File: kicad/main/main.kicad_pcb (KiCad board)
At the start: 2 copper layers, 20 parts, among them U1 DS1813-5+, U2 L7805, U3 Z80CPU, U4 74HC00, U5 AS6C4008-55PCN, U6 74HC273, U7 27C512, X1 4 MHz

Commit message: Smaller KiCad symbols, reset button
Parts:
- added SW1: Reset, Button_Switch_THT:SW_PUSH_6mm, F.Cu at (37.4, 99.3)
- added U5: 74HC00, Package_DIP:DIP-14_W7.62mm_Socket, F.Cu at (76.2, 114.3)
- moved C1 18.9 mm to (40.1, 45.7), turned to 180 degrees
- moved C4 12.8 mm to (119.4, 111.7)
- moved U4 12.8 mm to (99.1, 114.3)
- moved C2 2.58 mm to (30.5, 45.7)
- renumbered U5 to U6, U6 to U7, U7 to U8
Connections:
- U3 pad 27: unconnected-(U3-~{M1}-Pad27) -> ~{M1}
- U7 pad 11: ~{IORQ} -> IO~{EN}

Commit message: Basic PCB
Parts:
- added J1: Barrel_Jack_MountingPin, Connector_BarrelJack:BarrelJack_GCT_DCJ200-10-A_Horizontal, F.Cu at (157.2, 39.7)
- added RN3: 5K, Resistor_THT:R_Array_SIP9, F.Cu at (134.6, 106.7)
- added SW2: SW_DIP_x08, Button_Switch_THT:SW_DIP_SPSTx08_Slide_9.78x22.5mm_W7.62mm_P2.54mm, F.Cu at (137.2, 119.3)
- added U1: 74HC00, Package_DIP:DIP-14_W7.62mm_Socket, F.Cu at (86.4, 104.1)
- added U10: 74HC244, Package_DIP:DIP-20_W7.62mm_Socket, F.Cu at (134.5, 101.5)
- U9: renamed from U8; footprint Package_DIP:DIP-28_W15.24mm -> my:ZIF28
- moved C1 117.0 mm to (147.3, 38.1), turned to 180 degrees
- moved U7 107.0 mm to (139.7, 30.5)
- moved C9 97.4 mm to (137.2, 38.1), turned to 0 degrees
- moved X1 87.6 mm to (111.8, 90.2)
- moved C7 65.2 mm to (76.2, 91.4), turned to 180 degrees
- moved RN1 58.9 mm to (104.1, 88.9), turned to 180 degrees
- moved C8 48.4 mm to (73.7, 109.2)
- moved U5 48.4 mm to (73.7, 101.6)
- moved U4 45.4 mm to (94.0, 27.9)
- moved C2 45.4 mm to (99.1, 81.3)
- moved C4 43.1 mm to (121.9, 71.1), turned to 180 degrees
- moved U6 41.0 mm to (114.3, 27.9)
- moved BAR1 40.2 mm to (134.6, 86.4), turned to 90 degrees
- moved SW1 38.2 mm to (72.2, 114.9)
- moved RN2 37.8 mm to (134.6, 73.7), turned to 0 degrees
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- renumbered C2 to C1, C3 to C2, C4 to C3, C5 to C4, C6 to C5, C7 to C6, C8 to C7, C9 to C8, C1 to C9, U5 to U2, U4 to U3, U3 to U4, U1 to U5, U2 to U7, U7 to U8
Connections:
- net +9V renamed Net-(U7-IN)
- SW1 pad 1: unconnected-(SW1-Pad1) -> ~{RES}
- SW1 pad 2: ~{RES} -> GND
- U8 pad 11: IO~{EN} -> OUT~{EN}
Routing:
- net +5V: track 0.00 -> 159.2 mm
- net GND: track 0.00 -> 156.1 mm
- net Net-(U7-IN): track 0.00 -> 8.67 mm
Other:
- board outline added: 99.1 x 99.1 mm

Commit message: First PCB
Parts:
- removed U10: 74HC244, Package_DIP:DIP-20_W7.62mm_Socket
- removed U9: 27C512, my:ZIF28
- C1, C3, C4, C6, C7, C8: footprint Capacitor_THT:C_Disc_D3.0mm_W1.6mm_P2.50mm -> my:C_Disc_Long
- C2: footprint Capacitor_THT:C_Disc_D3.0mm_W1.6mm_P2.50mm -> my:C_Disc_Medium
- U1: value 74HC00 -> GAL16V8; footprint Package_DIP:DIP-14_W7.62mm_Socket -> Package_DIP:DIP-20_W7.62mm_Socket
- U2: value 74HC00 -> Z80CPU; footprint Package_DIP:DIP-14_W7.62mm_Socket -> Package_DIP:DIP-40_W15.24mm_Socket
- U3: value 74HC00 -> DS1813-5+; footprint Package_DIP:DIP-14_W7.62mm_Socket -> Package_TO_SOT_THT:TO-92
- U4: value Z80CPU -> AS6C4008-55PCN; footprint Package_DIP:DIP-40_W15.24mm_Socket -> Package_DIP:DIP-32_W15.24mm
- U5: value DS1813-5+ -> L7805; footprint Package_TO_SOT_THT:TO-92 -> Package_TO_SOT_THT:TO-220-3_Vertical
- U6: value AS6C4008-55PCN -> 74HC273; footprint Package_DIP:DIP-32_W15.24mm -> Package_DIP:DIP-20_W7.62mm_Socket
- U7: value L7805 -> 27C512; footprint Package_TO_SOT_THT:TO-220-3_Vertical -> my:ZIF28
- U8: value 74HC273 -> 74HC244
- moved U5 98.1 mm to (142.2, 31.4)
- moved U2 92.3 mm to (96.5, 27.9), turned to 0 degrees
- moved U6 76.2 mm to (100.3, 102.9), turned to 90 degrees
- moved U7 70.3 mm to (69.8, 38.1)
- moved C8 63.0 mm to (135.9, 99.1)
- moved U1 50.7 mm to (133.3, 85.1), turned to 90 degrees
- moved BAR1 48.5 mm to (100.3, 120.7)
- moved RN2 48.5 mm to (100.3, 108.0)
- moved C3 46.9 mm to (74.9, 99.1), turned to 0 degrees
- moved C1 44.7 mm to (135.9, 81.3), turned to 0 degrees
- moved U3 43.8 mm to (74.9, 116.8)
- moved X1 40.2 mm to (73.7, 102.9)
- moved U8 36.9 mm to (133.3, 102.9)
- moved C4 30.9 mm to (127.0, 40.6), turned to -90 degrees
- moved C2 27.9 mm to (99.1, 53.3)
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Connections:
- BAR1 pad 1: Net-(U8-Q0) -> Net-(U6-Q0)
- BAR1 pad 2: Net-(U8-Q1) -> Net-(U6-Q1)
- BAR1 pad 3: Net-(U8-Q2) -> Net-(U6-Q2)
- BAR1 pad 4: Net-(U8-Q3) -> Net-(U6-Q3)
- BAR1 pad 5: Net-(U8-Q4) -> Net-(U6-Q4)
- BAR1 pad 6: Net-(U8-Q5) -> Net-(U6-Q5)
- BAR1 pad 7: Net-(U8-Q6) -> Net-(U6-Q6)
- BAR1 pad 8: Net-(U8-Q7) -> Net-(U6-Q7)
- C9 pad 1: Net-(U7-IN) -> Net-(U5-IN)
- J1 pad 1: Net-(U7-IN) -> Net-(U5-IN)
- U1 pad 1: IO~{EN} -> unconnected-(U1-I1/CLK-Pad1)
- U1 pad 10: A_{0} -> GND
- U1 pad 11: OUT~{EN} -> GND
- U1 pad 12: A_{0} -> ROM~{EN}
- U1 pad 13: Net-(U1-Pad13) -> RAM~{EN}
- U1 pad 14: +5V -> unconnected-(U1-IO6-Pad14)
- U1 pad 2: IO~{EN} -> ~{MREQ}
- U1 pad 3: Net-(U1-Pad13) -> A_{0}
- U1 pad 4: Net-(U1-Pad13) -> A_{15}
- U1 pad 5: Net-(U1-Pad5) -> ~{IORQ}
- U1 pad 6: IN~{EN} -> ~{M1}
- U1 pad 7: GND -> unconnected-(U1-I7-Pad7)
- U1 pad 8: Net-(U1-Pad5) -> unconnected-(U1-I8-Pad8)
- U1 pad 9: A_{0} -> unconnected-(U1-I9-Pad9)
- U2 pad 1: ~{IORQ} -> A_{11}
- U2 pad 10: unconnected-(U2-Pad10) -> D_{6}
- U2 pad 11: unconnected-(U2-Pad11) -> +5V
- U2 pad 12: unconnected-(U2-Pad12) -> D_{2}
- U2 pad 13: unconnected-(U2-Pad13) -> D_{7}
- U2 pad 14: +5V -> D_{0}
- U2 pad 2: ~{IORQ} -> A_{12}
- U2 pad 3: Net-(U2-Pad3) -> A_{13}
- U2 pad 4: Net-(U2-Pad3) -> A_{14}
- U2 pad 5: ~{M1} -> A_{15}
- U2 pad 6: IO~{EN} -> CLK
- U2 pad 7: GND -> D_{4}
- U2 pad 8: unconnected-(U2-Pad8) -> D_{3}
- U2 pad 9: unconnected-(U2-Pad9) -> D_{5}
- U3 pad 1: ~{MREQ} -> ~{RES}
- U3 pad 2: ~{MREQ} -> +5V
- U3 pad 3: Net-(U3-Pad12) -> GND
- U4 pad 1: A_{11} -> unconnected-(U4-A18-Pad1)
- U4 pad 10: D_{6} -> A_{2}
- U4 pad 11: +5V -> A_{1}
- U4 pad 12: D_{2} -> A_{0}
- U4 pad 13: D_{7} -> D_{0}
- U4 pad 14: D_{0} -> D_{1}
- U4 pad 15: D_{1} -> D_{2}
- U4 pad 16: Net-(RN1-R3) -> GND
- U4 pad 17: Net-(RN1-R4) -> D_{3}
- U4 pad 18: unconnected-(U4-~{HALT}-Pad18) -> D_{4}
- U4 pad 19: ~{MREQ} -> D_{5}
- U4 pad 2: A_{12} -> unconnected-(U4-A16-Pad2)
- U4 pad 20: ~{IORQ} -> D_{6}
- U4 pad 21: ~{RD} -> D_{7}
- U4 pad 22: ~{WD} -> RAM~{EN}
- U4 pad 23: unconnected-(U4-~{BUSACK}-Pad23) -> A_{10}
- U4 pad 24: Net-(RN1-R2) -> ~{RD}
- U4 pad 25: Net-(RN1-R1) -> A_{11}
- U4 pad 26: ~{RES} -> A_{9}
- U4 pad 27: ~{M1} -> A_{8}
- U4 pad 28: unconnected-(U4-~{RFSH}-Pad28) -> A_{13}
- U4 pad 29: GND -> ~{WD}
- U4 pad 3: A_{13} -> A_{14}
- U4 pad 30: A_{0} -> unconnected-(U4-A17-Pad30)
- U4 pad 31: A_{1} -> unconnected-(U4-A15-Pad31)
- U4 pad 32: A_{2} -> +5V
- U4 pad 4: A_{14} -> A_{12}
- U4 pad 5: A_{15} -> A_{7}
- U4 pad 6: CLK -> A_{6}
- U4 pad 7: D_{4} -> A_{5}
- U4 pad 8: D_{3} -> A_{4}
- U4 pad 9: D_{5} -> A_{3}
- U5 pad 1: ~{RES} -> Net-(U5-IN)
- U5 pad 2: +5V -> GND
- U5 pad 3: GND -> +5V
- U6 pad 1: unconnected-(U6-A18-Pad1) -> ~{RES}
- U6 pad 10: A_{2} -> GND
- U6 pad 11: A_{1} -> OUT~{EN}
- U6 pad 12: A_{0} -> Net-(U6-Q4)
- U6 pad 13: D_{0} -> D_{4}
- U6 pad 14: D_{1} -> D_{5}
- U6 pad 15: D_{2} -> Net-(U6-Q5)
- U6 pad 16: GND -> Net-(U6-Q6)
- U6 pad 17: D_{3} -> D_{6}
- U6 pad 18: D_{4} -> D_{7}
- U6 pad 19: D_{5} -> Net-(U6-Q7)
- U6 pad 2: unconnected-(U6-A16-Pad2) -> Net-(U6-Q0)
- U6 pad 20: D_{6} -> +5V
- U6 pad 3: A_{14} -> D_{0}
- U6 pad 4: A_{12} -> D_{1}
- U6 pad 5: A_{7} -> Net-(U6-Q1)
- U6 pad 6: A_{6} -> Net-(U6-Q2)
- U6 pad 7: A_{5} -> D_{2}
- U6 pad 8: A_{4} -> D_{3}
- U6 pad 9: A_{3} -> Net-(U6-Q3)
- U7 pad 1: Net-(U7-IN) -> unconnected-(U7-A15-Pad1)
- U7 pad 2: GND -> A_{12}
- U7 pad 3: +5V -> A_{7}
- U8 pad 1: ~{RES} -> IN~{EN}
- U8 pad 11: OUT~{EN} -> Net-(RN3-R8)
- U8 pad 12: Net-(U8-Q4) -> D_{3}
- U8 pad 13: D_{4} -> Net-(RN3-R7)
- U8 pad 14: D_{5} -> D_{2}
- U8 pad 15: Net-(U8-Q5) -> Net-(RN3-R6)
- U8 pad 16: Net-(U8-Q6) -> D_{1}
- U8 pad 17: D_{6} -> Net-(RN3-R5)
- U8 pad 18: D_{7} -> D_{0}
- U8 pad 19: Net-(U8-Q7) -> IN~{EN}
- U8 pad 2: Net-(U8-Q0) -> Net-(RN3-R1)
- U8 pad 3: D_{0} -> D_{4}
- U8 pad 4: D_{1} -> Net-(RN3-R2)
- U8 pad 5: Net-(U8-Q1) -> D_{5}
- U8 pad 6: Net-(U8-Q2) -> Net-(RN3-R3)
- U8 pad 7: D_{2} -> D_{6}
- U8 pad 8: D_{3} -> Net-(RN3-R4)
- U8 pad 9: Net-(U8-Q3) -> D_{7}
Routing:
- net GND: track 156.1 -> 82.4 mm
- net +5V: track 159.2 -> 88.9 mm
- net Net-(U7-IN): track 8.67 -> 0.00 mm
- net Net-(U5-IN): track 0.00 -> 7.50 mm

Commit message: PCB update + Gerber
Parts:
- added H1: MountingHole, MountingHole:MountingHole_3.2mm_M3_Pad, F.Cu at (67.3, 29.2)
- added H2: MountingHole, MountingHole:MountingHole_3.2mm_M3_Pad, F.Cu at (158.8, 29.2)
- added H3: MountingHole, MountingHole:MountingHole_3.2mm_M3_Pad, F.Cu at (67.3, 120.7)
- added H4: MountingHole, MountingHole:MountingHole_3.2mm_M3_Pad, F.Cu at (158.8, 120.7)
- moved J1 11.7 mm to (148.6, 47.6), turned to 90 degrees
- moved C7 7.62 mm to (83.8, 88.9)
- moved U7 7.62 mm to (69.8, 45.7)
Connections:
- U1 pad 1: unconnected-(U1-I1/CLK-Pad1) -> +5V
- U1 pad 7: unconnected-(U1-I7-Pad7) -> GND
- U1 pad 8: unconnected-(U1-I8-Pad8) -> GND
- U1 pad 9: unconnected-(U1-I9-Pad9) -> GND
- U4 pad 1: unconnected-(U4-A18-Pad1) -> GND
- U4 pad 2: unconnected-(U4-A16-Pad2) -> GND
- U4 pad 30: unconnected-(U4-A17-Pad30) -> GND
- U4 pad 31: unconnected-(U4-A15-Pad31) -> GND
- U7 pad 1: unconnected-(U7-A15-Pad1) -> GND
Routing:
- net GND: track 82.4 -> 160.7 mm
- net +5V: track 88.9 -> 93.8 mm

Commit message: Final v1 PCB
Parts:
- moved U1 165.4 mm to (95.2, -75.9), turned to 0 degrees
- moved C1 159.0 mm to (99.1, -73.4), turned to -90 degrees
- moved C3 144.8 mm to (17.8, -34.0)
- moved X1 144.8 mm to (16.5, -30.2)
- moved BAR1 144.5 mm to (47.0, -13.7)
- moved C5 144.5 mm to (95.2, -96.2)
- moved C6 144.5 mm to (49.5, -35.3)
- moved C8 144.5 mm to (82.6, -35.3)
- moved C9 144.5 mm to (86.9, -96.2)
- moved H1 144.5 mm to (14.0, -105.1)
- moved H2 144.5 mm to (105.4, -105.1)
- moved H3 144.5 mm to (14.0, -13.7)
- moved H4 144.5 mm to (105.4, -13.7)
- moved RN2 144.5 mm to (47.0, -26.4)
- moved U2 144.5 mm to (43.2, -106.4)
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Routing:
- net GND: track 160.7 -> 208.9 mm
- net +5V: track 93.8 -> 132.6 mm
- net ~{RES}: track 0.00 -> 13.1 mm
- net Net-(U5-IN): track 7.50 -> 20.5 mm
- net Net-(RN3-R7): track 0.00 -> 6.02 mm
- net Net-(RN3-R6): track 0.00 -> 6.02 mm
- net Net-(RN3-R4): track 0.00 -> 6.02 mm
- net Net-(RN3-R2): track 0.00 -> 6.02 mm
- net Net-(RN3-R8): track 0.00 -> 6.02 mm
- net Net-(RN3-R5): track 0.00 -> 6.02 mm
- net Net-(RN3-R3): track 0.00 -> 6.02 mm
- net Net-(RN3-R1): track 0.00 -> 6.02 mm
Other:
- board text added: "Версія 1"
- board text added: "Виготовлено у Львові липень 2023"
- board text added: "ЛЕО-80"

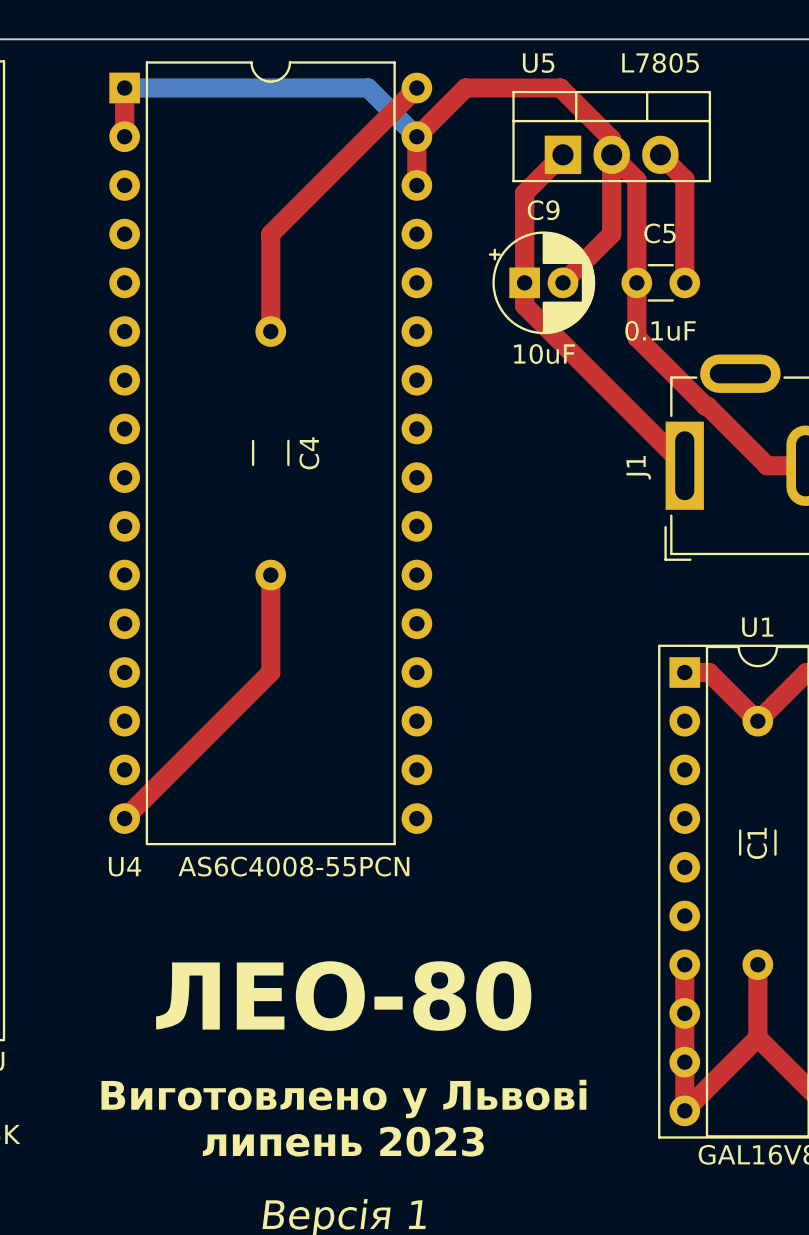
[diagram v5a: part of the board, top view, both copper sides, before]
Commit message: Fix RAM CE2, add /RFSH
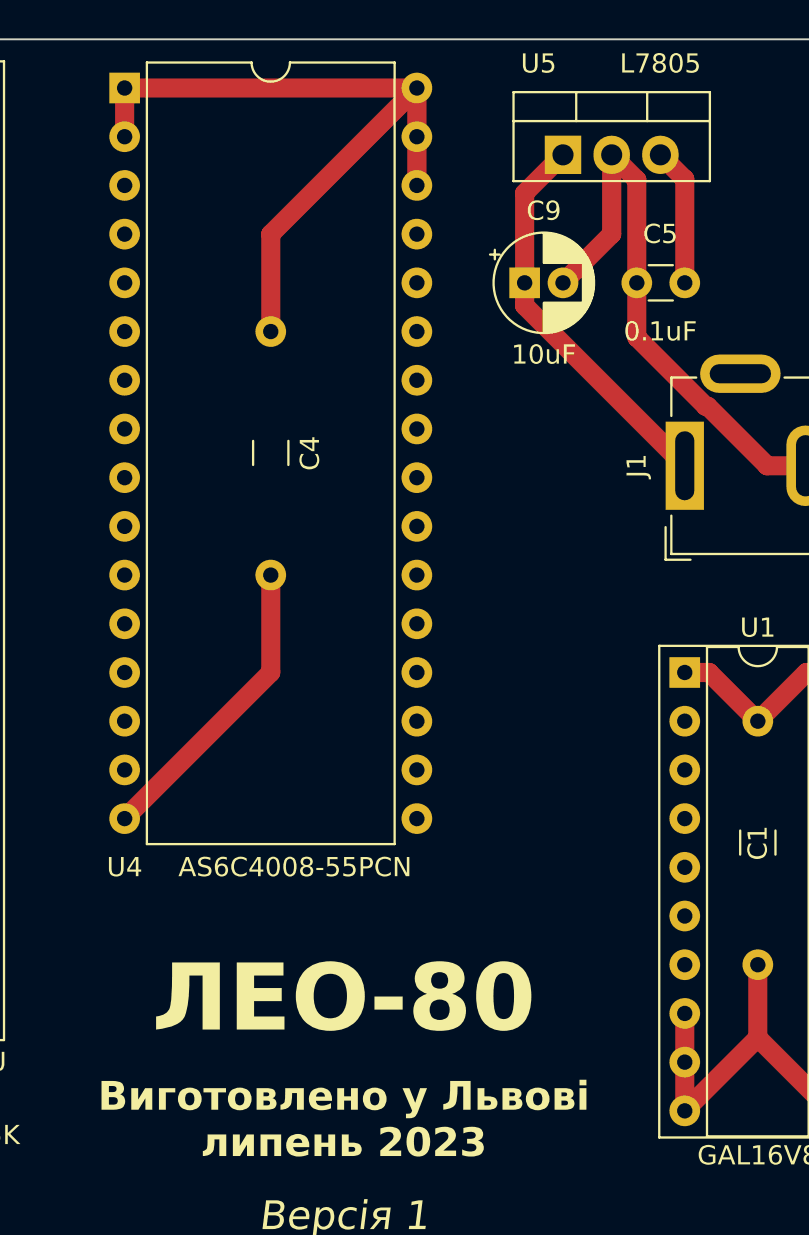
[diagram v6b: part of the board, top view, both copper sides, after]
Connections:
- U1 pad 7: GND -> ~{RFSH}
- U2 pad 28: unconnected-(U2-~{RFSH}-Pad28) -> ~{RFSH}
- U4 pad 1: GND -> +5V
- U4 pad 2: GND -> +5V
- U4 pad 30: GND -> +5V
- U4 pad 31: GND -> +5V
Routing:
- net GND: track 208.9 -> 171.9 mm
- net +5V: track 132.6 -> 155.4 mm
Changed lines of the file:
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@@
   (net 76 "unconnected-(U2-~{HALT}-Pad18)")
   (net 77 "unconnected-(U2-~{BUSACK}-Pad23)")
-  (net 78 "unconnected-(U2-~{RFSH}-Pad28)")
+  (net 78 "~{RFSH}")
   (footprint "MountingHole:MountingHole_3.2mm_M3_Pad" (layer "F.Cu")
     (at 105.41 -105.12)
@@
       (stroke (width 0.1) (type solid)) (layer "F.Fab"))
     (pad "1" thru_hole rect (at 0 0) (size 1.6 1.6) (drill 0.8) (layers "*.Cu" "*.Mask")
-      (net 21 "GND") (pinfunction "A18") (pintype "input"))
+      (net 22 "+5V") (pinfunction "A18") (pintype "input"))
     (pad "2" thru_hole oval (at 0 2.54) (size 1.6 1.6) (drill 0.8) (layers "*.Cu" "*.Mask")
-      (net 21 "GND") (pinfunction "A16") (pintype "input"))
+      (net 22 "+5V") (pinfunction "A16") (pintype "input"))
     (pad "3" thru_hole oval (at 0 5.08) (size 1.6 1.6) (drill 0.8) (layers "*.Cu" "*.Mask")
       (net 31 "A_{14}") (pinfunction "A14") (pintype "input"))
@@
       (net 46 "~{WD}") (pinfunction "WE#") (pintype "input"))
     (pad "30" thru_hole oval (at 15.24 5.08) (size 1.6 1.6) (drill 0.8) (layers "*.Cu" "*.Mask")
-      (net 21 "GND") (pinfunction "A17") (pintype "input"))
+      (net 22 "+5V") (pinfunction "A17") (pintype "input"))
     (pad "31" thru_hole oval (at 15.24 2.54) (size 1.6 1.6) (drill 0.8) (layers "*.Cu" "*.Mask")
-      (net 21 "GND") (pinfunction "A15") (pintype "input"))
+      (net 22 "+5V") (pinfunction "A15") (pintype "input"))
     (pad "32" thru_hole oval (at 15.24 0) (size 1.6 1.6) (drill 0.8) (layers "*.Cu" "*.Mask")
       (net 22 "+5V") (pinfunction "VCC") (pintype "power_in"))
@@
       (net 65 "~{M1}") (pinfunction "~{M1}") (pintype "output"))
     (pad "28" thru_hole oval (at 15.24 30.48) (size 1.6 1.6) (drill 0.8) (layers "*.Cu" "*.Mask")
-      (net 78 "unconnected-(U2-~{RFSH}-Pad28)") (pinfunction "~{RFSH}") (pintype "output+no_connect"))
+      (net 78 "~{RFSH}") (pinfunction "~{RFSH}") (pintype "output"))
     (pad "29" thru_hole oval (at 15.24 27.94) (size 1.6 1.6) (drill 0.8) (layers "*.Cu" "*.Mask")
       (net 21 "GND") (pinfunction "GND") (pintype "power_in"))
@@
       (net 65 "~{M1}") (pinfunction "I6") (pintype "input"))
     (pad "7" thru_hole oval (at 0 15.24) (size 1.6 1.6) (drill 0.8) (layers "*.Cu" "*.Mask")
-      (net 21 "GND") (pinfunction "I7") (pintype "input"))
+      (net 78 "~{RFSH}") (pinfunction "I7") (pintype "input"))
     (pad "8" thru_hole oval (at 0 17.78) (size 1.6 1.6) (drill 0.8) (layers "*.Cu" "*.Mask")
       (net 21 "GND") (pinfunction "I8") (pintype "input"))
@@
   )
   (segment (start 92.75 -96.23) (end 92.75 -101.595) (width 1) (layer "F.Cu") (net 21))
-  (segment (start 81.28 -103.85) (end 83.82 -106.39) (width 1) (layer "F.Cu") (net 21))
   (segment (start 99.06 -56.86) (end 99.06 -60.67) (width 1) (layer "F.Cu") (net 21))
   (segment (start 31.75 -32.73) (end 30.48 -34) (width 1) (layer "F.Cu") (net 21))
   (segment (start 37.54 -13.97) (end 31.04 -13.97) (width 1) (layer "F.Cu") (net 21))
   (segment (start 55.9 -80.99) (end 55.9 -80.97) (width 1) (layer "F.Cu") (net 21))
-  (segment (start 66.04 -106.39) (end 66.04 -103.85) (width 1) (layer "F.Cu") (net 21))
   (segment (start 16.51 -55.59) (end 12.7 -59.4) (width 1) (layer "F.Cu") (net 21))
   (segment (start 73.66 -80.99) (end 73.66 -75.91) (width 1) (layer "F.Cu") (net 21))
   (segment (start 102.87 -31.46) (end 99.06 -35.27) (width 1) (layer "F.Cu") (net 21))
-  (segment (start 91.44 -103.7175) (end 91.44 -102.905) (width 1) (layer "F.Cu") (net 21))
   (segment (start 73.66 -75.91) (end 66.04 -68.29) (width 1) (layer "F.Cu") (net 21))
   (segment (start 101.55 -86.69) (end 99.55 -86.69) (width 1) (layer "F.Cu") (net 21))
@@
   (segment (start 12.7 -59.4) (end 12.7 -84.8) (width 1) (layer "F.Cu") (net 21))
   (segment (start 99.55 -86.69) (end 96.45 -89.79) (width 1) (layer "F.Cu") (net 21))
-  (segment (start 81.28 -103.85) (end 81.28 -101.31) (width 1) (layer "F.Cu") (net 21))
   (segment (start 31.04 -13.97) (end 23.731141 -13.97) (width 0.25) (layer "F.Cu") (net 21))
   (segment (start 99.06 -35.27) (end 95.27 -35.27) (width 1) (layer "F.Cu") (net 21))
   (segment (start 92.75 -101.595) (end 91.44 -102.905) (width 1) (layer "F.Cu") (net 21))
+  (segment (start 95.25 -53.05) (end 95.25 -58.13) (width 1) (layer "F.Cu") (net 21))
   (segment (start 69.85 -31.46) (end 66.04 -35.27) (width 1) (layer "F.Cu") (net 21))
   (segment (start 92.75 -93.385837) (end 92.75 -96.23) (width 1) (layer "F.Cu") (net 21))
   (segment (start 17.78 -45.43) (end 17.78 -54.32) (width 1) (layer "F.Cu") (net 21))
-  (segment (start 88.7675 -106.39) (end 91.44 -103.7175) (width 1) (layer "F.Cu") (net 21))
   (segment (start 22.86 -14.841141) (end 22.86 -16.22) (width 0.25) (layer "F.Cu") (net 21))
   (segment (start 91.44 -102.905) (end 91.44 -98.77) (width 1) (layer "F.Cu") (net 21))
@@
   (segment (start 55.9 -80.97) (end 58.42 -78.45) (width 1) (layer "F.Cu") (net 21))
   (segment (start 12.7 -84.8) (end 16.51 -88.61) (width 1) (layer "F.Cu") (net 21))
-  (segment (start 95.25 -53.05) (end 95.25 -60.67) (width 1) (layer "F.Cu") (net 21))
   (segment (start 99.06 -56.86) (end 102.87 -53.05) (width 1) (layer "F.Cu") (net 21))
   (segment (start 96.45 -89.79) (end 96.345837 -89.79) (width 1) (layer "F.Cu") (net 21))
-  (segment (start 83.82 -106.39) (end 88.7675 -106.39) (width 1) (layer "F.Cu") (net 21))
-  (segment (start 78.74 -106.39) (end 81.28 -103.85) (width 1) (layer "B.Cu") (net 21))
   (segment (start 30.48 -34) (end 29.21 -34) (width 1) (layer "B.Cu") (net 21))
   (segment (start 29.21 -34) (end 17.78 -45.43) (width 1) (layer "B.Cu") (net 21))
-  (segment (start 66.04 -106.39) (end 78.74 -106.39) (width 1) (layer "B.Cu") (net 21))
   (segment (start 29.680001 -86.540001) (end 31.75 -88.61) (width 1) (layer "F.Cu") (net 22))
   (segment (start 22.86 -37.81) (end 30.48 -45.43) (width 1) (layer "F.Cu") (net 22))
@@
   (segment (start 73.66 -98.77) (end 81.28 -106.39) (width 1) (layer "F.Cu") (net 22))
   (segment (start 95.25 -75.91) (end 96.52 -75.91) (width 1) (layer "F.Cu") (net 22))
+  (segment (start 66.04 -106.39) (end 66.04 -103.85) (width 1) (layer "F.Cu") (net 22))
   (segment (start 24.13 -27.65) (end 17.78 -34) (width 0.25) (layer "F.Cu") (net 22))
   (segment (start 30.48 -45.43) (end 29.680001 -46.229999) (width 1) (layer "F.Cu") (net 22))
@@
   (segment (start 73.66 -93.69) (end 73.66 -98.77) (width 1) (layer "F.Cu") (net 22))
   (segment (start 102.87 -75.91) (end 101.6 -75.91) (width 1) (layer "F.Cu") (net 22))
+  (segment (start 66.04 -106.39) (end 81.28 -106.39) (width 1) (layer "F.Cu") (net 22))
   (segment (start 95.25 -101.635) (end 93.98 -102.905) (width 1) (layer "F.Cu") (net 22))
   (segment (start 80.01 -39.08) (end 80.01 -37.83) (width 1) (layer "F.Cu") (net 22))
@@
   (segment (start 46.99 -37.81) (end 49.53 -35.27) (width 1) (layer "F.Cu") (net 22))
   (segment (start 16.51 -37.81) (end 16.51 -35.27) (width 1) (layer "F.Cu") (net 22))
+  (segment (start 81.28 -106.39) (end 81.28 -101.31) (width 1) (layer "F.Cu") (net 22))
   (segment (start 37.54 -18.47) (end 31.04 -18.47) (width 1) (layer "F.Cu") (net 27))
   (segment (start 27.65 -18.47) (end 25.4 -16.22) (width 0.25) (layer "F.Cu") (net 27))
@@
       5920eb2e-23ec-479e-aa8d-9807e336ef53
       7bfaba82-eb10-408a-910e-f19fd6a5c2e6
+      aa143f62-9af2-4690-8621-7863b4b43ce5
       b6096c56-f94f-4d8b-87a9-3ab4fec251d4
       d64931d2-b4a6-4a3c-af8a-09203eebfe1d
-      e483a733-b905-4083-ba0a-671c49adc041
       f30197eb-17e9-4c99-b0aa-0cf59526a2f4
       f61a0d70-468c-45b5-bea5-dd504bcbcfec
